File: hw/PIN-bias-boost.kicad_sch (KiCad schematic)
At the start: 9 parts, among them U2101 LT8330ES6-TRMPBF

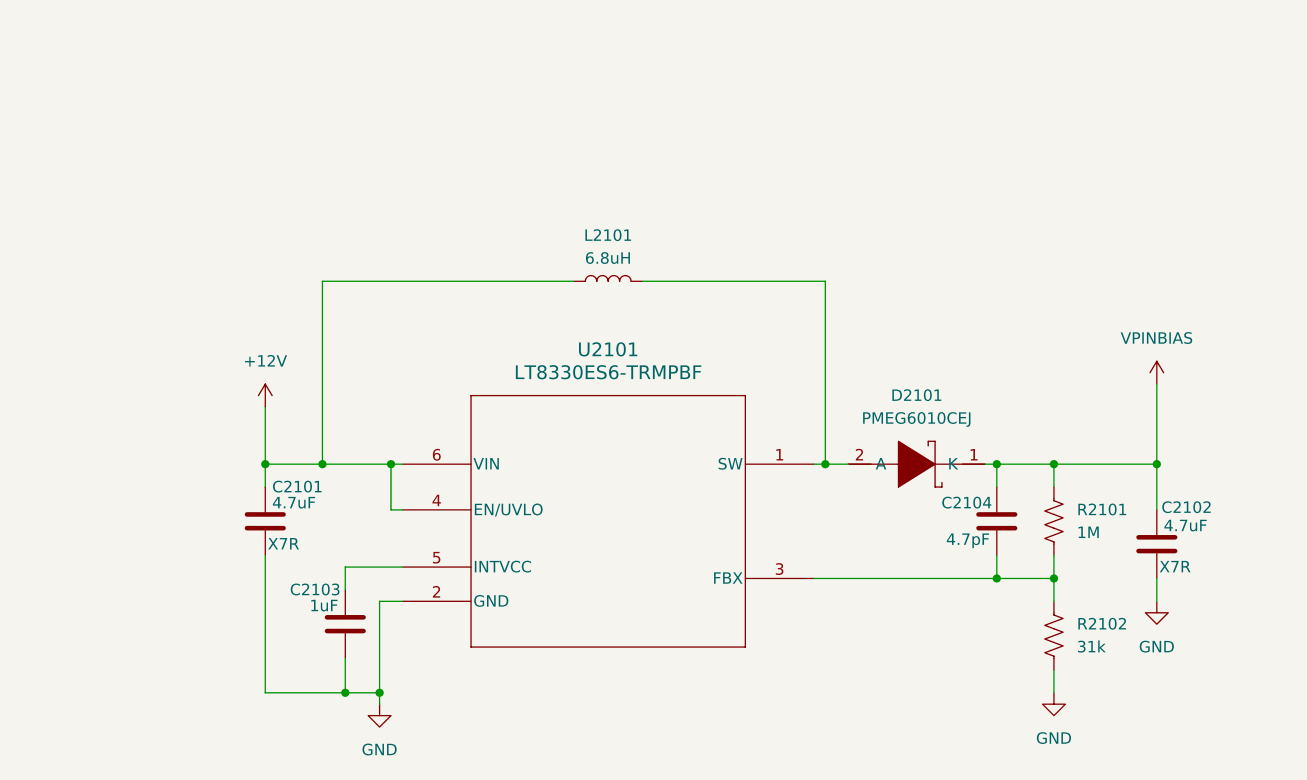
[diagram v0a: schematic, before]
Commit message: Add EER tank calculations stuff
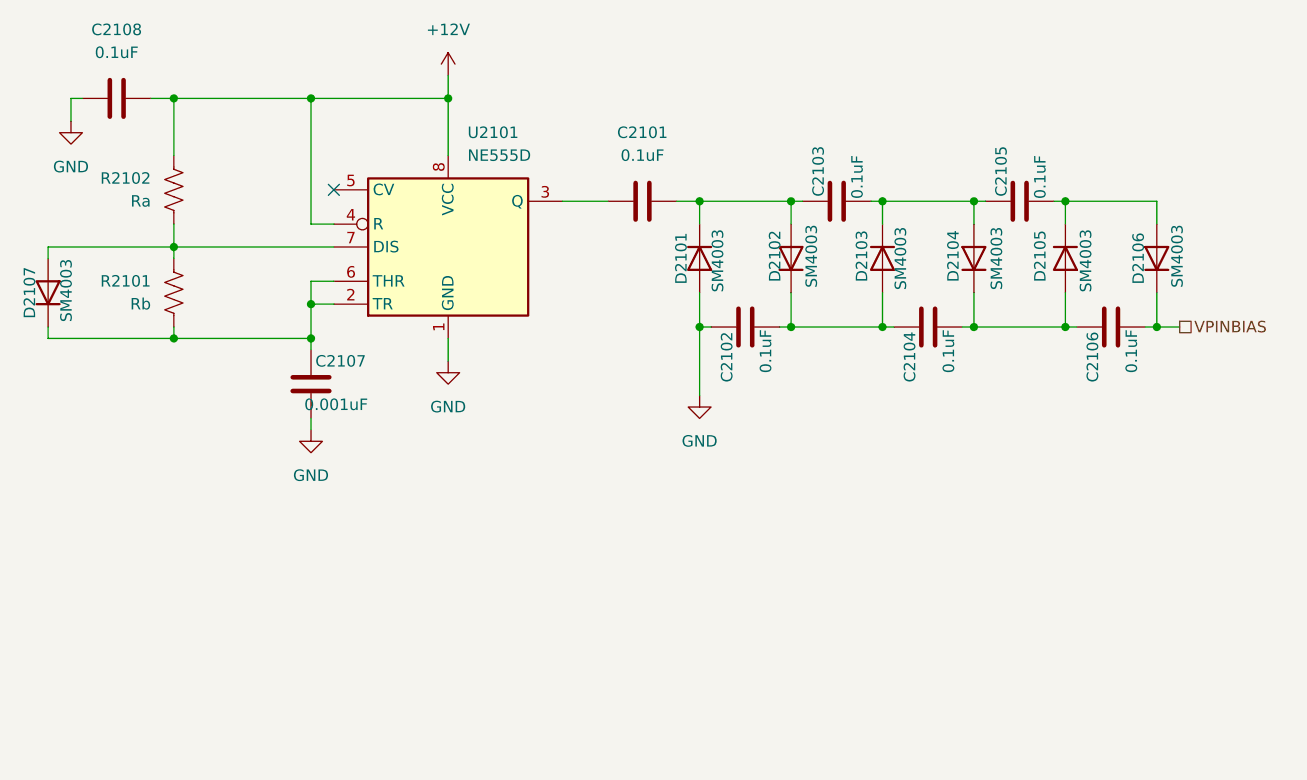
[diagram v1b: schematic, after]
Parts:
- removed D2101: PMEG6010CEJ, symbol USB-SSB-txcvr-altium-import:root_1_Df_TI WEBENCH
- removed L2101: 6.8uH, symbol Device:L
- removed U2101: LT8330ES6-TRMPBF, TSOT-23_S6_LIT, symbol LT8330ES6-TRMPBF:LT8330ES6-TRMPBF
- added C2105, C2106, C2108: 0.1uF, symbol Device:C
- added C2107: 0.001uF, symbol Device:C
- added D2101, D2102, D2103, D2104, D2105, D2106, D2107: SM4003, Diode_SMD:D_MELF, symbol Diode:SM4003
- added U2101: NE555D, Package_SO:SOIC-8_3.9x4.9mm_P1.27mm, symbol Timer:NE555D
- C2101, C2102: value 4.7uF -> 0.1uF; cap-type X7R -> (none)
- C2103: value 1uF -> 0.1uF
- C2104: value 4.7pF -> 0.1uF
- R2101: value 1M -> Rb
- R2102: value 31k -> Ra
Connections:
- net +12V: now also R2102.1, C2108.2, U2101.4 (R), U2101.8 (VCC); no longer C2101.1
- net GND: now also C2107.2, C2108.1, D2101.2 (A), U2101.1 (GND); no longer C2101.2, C2103.2, R2102.2
- net VPINBIAS: now also C2106.1, D2106.1 (K); no longer C2102.1, C2104.1, R2101.1
- net at C2103.1: now also C2105.2, D2103.1 (K), D2104.2 (A)
- new net: C2107.1, D2107.1 (K), R2101.2, U2101.2 (TR), U2101.6 (THR)
- new net: C2101.2, C2103.2, D2101.1 (K), D2102.2 (A)
- new net: D2107.2 (A), R2101.1, R2102.2, U2101.7 (DIS)
- new net: C2101.1, U2101.3 (Q)
- new net: C2104.1, C2106.2, D2104.1 (K), D2105.2 (A)
- new net: C2102.1, C2104.2, D2102.1 (K), D2103.2 (A)
- new net: C2105.1, D2105.1 (K), D2106.2 (A)
- no-connect marks 0 -> 1

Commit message: Tx LPF and its selection is pretty much done. Fix some OCD. Start to describe the design and construction.
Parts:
- renumbered C2108 to C2101, C2107 to C2102, C2101 to C2103, C2102 to C2104, C2103 to C2105, C2104 to C2106, C2105 to C2107, C2106 to C2108, D2107 to D2101, D2101 to D2102, D2102 to D2103, D2103 to D2104, D2104 to D2105, D2105 to D2106, D2106 to D2107, R2102 to R2101, R2101 to R2102
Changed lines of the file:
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@@
 		(on_board yes)
 		(dnp no)
-		(property "Reference" "C2107"
+		(property "Reference" "C2102"
 			(at 136.652 86.36 0)
 			(effects
@@
 			(project "USB-SSB-txcvr"
 				(path "/8ae46c04-d01a-4756-8774-512b694bfaff/cbf7569b-90aa-4e1a-84a7-d4153f6242b6/f249c9f1-932d-476f-a809-68b4c7a5d791"
-					(reference "C2107")
+					(reference "C2102")
 					(unit 1)
 				)
@@
 		(on_board yes)
 		(dnp no)
-		(property "Reference" "C2103"
+		(property "Reference" "C2105"
 			(at 189.738 68.072 0)
 			(effects
@@
 			(project "USB-SSB-txcvr"
 				(path "/8ae46c04-d01a-4756-8774-512b694bfaff/cbf7569b-90aa-4e1a-84a7-d4153f6242b6/f249c9f1-932d-476f-a809-68b4c7a5d791"
-					(reference "C2103")
+					(reference "C2105")
 					(unit 1)
 				)
@@
 		(on_board yes)
 		(dnp no)
-		(property "Reference" "D2107"
+		(property "Reference" "D2101"
 			(at 102.108 78.74 0)
 			(effects
@@
 			(project "USB-SSB-txcvr"
 				(path "/8ae46c04-d01a-4756-8774-512b694bfaff/cbf7569b-90aa-4e1a-84a7-d4153f6242b6/f249c9f1-932d-476f-a809-68b4c7a5d791"
-					(reference "D2107")
+					(reference "D2101")
 					(unit 1)
 				)
@@
 		(on_board yes)
 		(dnp no)
-		(property "Reference" "C2106"
+		(property "Reference" "C2108"
 			(at 220.218 83.058 0)
 			(effects
@@
 			(project "USB-SSB-txcvr"
 				(path "/8ae46c04-d01a-4756-8774-512b694bfaff/cbf7569b-90aa-4e1a-84a7-d4153f6242b6/f249c9f1-932d-476f-a809-68b4c7a5d791"
-					(reference "C2106")
+					(reference "C2108")
 					(unit 1)
 				)
@@
 		(dnp no)
 		(fields_autoplaced yes)
-		(property "Reference" "#PWR02102"
+		(property "Reference" "#PWR02103"
 			(at 148.59 58.42 0)
 			(effects
@@
 			(project ""
 				(path "/8ae46c04-d01a-4756-8774-512b694bfaff/cbf7569b-90aa-4e1a-84a7-d4153f6242b6/f249c9f1-932d-476f-a809-68b4c7a5d791"
-					(reference "#PWR02102")
+					(reference "#PWR02103")
 					(unit 1)
 				)
@@
 		(on_board yes)
 		(dnp no)
-		(property "Reference" "D2102"
+		(property "Reference" "D2103"
 			(at 184.912 74.676 0)
 			(effects
@@
 			(project "USB-SSB-txcvr"
 				(path "/8ae46c04-d01a-4756-8774-512b694bfaff/cbf7569b-90aa-4e1a-84a7-d4153f6242b6/f249c9f1-932d-476f-a809-68b4c7a5d791"
-					(reference "D2102")
+					(reference "D2103")
 					(unit 1)
 				)
@@
 		(on_board yes)
 		(dnp no)
-		(property "Reference" "D2106"
+		(property "Reference" "D2107"
 			(at 225.298 74.93 0)
 			(effects
@@
 			(project "USB-SSB-txcvr"
 				(path "/8ae46c04-d01a-4756-8774-512b694bfaff/cbf7569b-90aa-4e1a-84a7-d4153f6242b6/f249c9f1-932d-476f-a809-68b4c7a5d791"
-					(reference "D2106")
+					(reference "D2107")
 					(unit 1)
 				)
@@
 		(dnp no)
 		(fields_autoplaced yes)
-		(property "Reference" "#PWR02105"
+		(property "Reference" "#PWR02101"
 			(at 106.68 66.04 0)
 			(effects
@@
 			(project "USB-SSB-txcvr"
 				(path "/8ae46c04-d01a-4756-8774-512b694bfaff/cbf7569b-90aa-4e1a-84a7-d4153f6242b6/f249c9f1-932d-476f-a809-68b4c7a5d791"
-					(reference "#PWR02105")
+					(reference "#PWR02101")
 					(unit 1)
 				)
@@
 		(dnp no)
 		(fields_autoplaced yes)
-		(property "Reference" "C2101"
+		(property "Reference" "C2103"
 			(at 170.18 60.96 90)
 			(effects
@@
 			(project ""
 				(path "/8ae46c04-d01a-4756-8774-512b694bfaff/cbf7569b-90aa-4e1a-84a7-d4153f6242b6/f249c9f1-932d-476f-a809-68b4c7a5d791"
-					(reference "C2101")
+					(reference "C2103")
 					(unit 1)
 				)
@@
 		(on_board yes)
 		(dnp no)
-		(property "Reference" "C2104"
+		(property "Reference" "C2106"
 			(at 199.898 83.058 0)
 			(effects
@@
 			(project "USB-SSB-txcvr"
 				(path "/8ae46c04-d01a-4756-8774-512b694bfaff/cbf7569b-90aa-4e1a-84a7-d4153f6242b6/f249c9f1-932d-476f-a809-68b4c7a5d791"
-					(reference "C2104")
+					(reference "C2106")
 					(unit 1)
 				)
@@
 		(on_board yes)
 		(dnp no)
-		(property "Reference" "D2105"
+		(property "Reference" "D2106"
 			(at 214.376 74.676 0)
 			(effects
@@
 			(project "USB-SSB-txcvr"
 				(path "/8ae46c04-d01a-4756-8774-512b694bfaff/cbf7569b-90aa-4e1a-84a7-d4153f6242b6/f249c9f1-932d-476f-a809-68b4c7a5d791"
-					(reference "D2105")
+					(reference "D2106")
 					(unit 1)
 				)
@@
 		(on_board yes)
 		(dnp no)
-		(property "Reference" "D2103"
+		(property "Reference" "D2104"
 			(at 194.564 74.676 0)
 			(effects
@@
 			(project "USB-SSB-txcvr"
 				(path "/8ae46c04-d01a-4756-8774-512b694bfaff/cbf7569b-90aa-4e1a-84a7-d4153f6242b6/f249c9f1-932d-476f-a809-68b4c7a5d791"
-					(reference "D2103")
+					(reference "D2104")
 					(unit 1)
 				)
@@
 		(on_board yes)
 		(dnp no)
-		(property "Reference" "C2105"
+		(property "Reference" "C2107"
 			(at 210.058 68.072 0)
 			(effects
@@
 			(project "USB-SSB-txcvr"
 				(path "/8ae46c04-d01a-4756-8774-512b694bfaff/cbf7569b-90aa-4e1a-84a7-d4153f6242b6/f249c9f1-932d-476f-a809-68b4c7a5d791"
-					(reference "C2105")
+					(reference "C2107")
 					(unit 1)
 				)
@@
 		(on_board yes)
 		(dnp no)
-		(property "Reference" "D2101"
+		(property "Reference" "D2102"
 			(at 174.498 74.93 0)
 			(effects
@@
 			(project ""
 				(path "/8ae46c04-d01a-4756-8774-512b694bfaff/cbf7569b-90aa-4e1a-84a7-d4153f6242b6/f249c9f1-932d-476f-a809-68b4c7a5d791"
-					(reference "D2101")
+					(reference "D2102")
 					(unit 1)
 				)
@@
 		(dnp no)
 		(fields_autoplaced yes)
-		(property "Reference" "#PWR02101"
+		(property "Reference" "#PWR02105"
 			(at 176.53 96.52 0)
 			(effects
@@
 			(project ""
 				(path "/8ae46c04-d01a-4756-8774-512b694bfaff/cbf7569b-90aa-4e1a-84a7-d4153f6242b6/f249c9f1-932d-476f-a809-68b4c7a5d791"
-					(reference "#PWR02101")
+					(reference "#PWR02105")
 					(unit 1)
 				)
@@
 		(dnp no)
 		(fields_autoplaced yes)
-		(property "Reference" "#PWR02104"
+		(property "Reference" "#PWR02102"
 			(at 133.35 100.33 0)
 			(effects
@@
 			(project "USB-SSB-txcvr"
 				(path "/8ae46c04-d01a-4756-8774-512b694bfaff/cbf7569b-90aa-4e1a-84a7-d4153f6242b6/f249c9f1-932d-476f-a809-68b4c7a5d791"
-					(reference "#PWR02104")
+					(reference "#PWR02102")
 					(unit 1)
 				)
@@
 		(on_board yes)
 		(dnp no)
-		(property "Reference" "R2101"
+		(property "Reference" "R2102"
 			(at 115.57 77.4699 0)
 			(effects
@@
 			(project ""
 				(path "/8ae46c04-d01a-4756-8774-512b694bfaff/cbf7569b-90aa-4e1a-84a7-d4153f6242b6/f249c9f1-932d-476f-a809-68b4c7a5d791"
-					(reference "R2101")
+					(reference "R2102")
 					(unit 1)
 				)
@@
 		(dnp no)
 		(fields_autoplaced yes)
-		(property "Reference" "#PWR02103"
+		(property "Reference" "#PWR02104"
 			(at 148.59 92.71 0)
 			(effects
@@
 			(project "USB-SSB-txcvr"
 				(path "/8ae46c04-d01a-4756-8774-512b694bfaff/cbf7569b-90aa-4e1a-84a7-d4153f6242b6/f249c9f1-932d-476f-a809-68b4c7a5d791"
-					(reference "#PWR02103")
+					(reference "#PWR02104")
 					(unit 1)
 				)
@@
 		(on_board yes)
 		(dnp no)
-		(property "Reference" "C2102"
+		(property "Reference" "C2104"
 			(at 179.578 83.058 0)
 			(effects
@@
 			(project "USB-SSB-txcvr"
 				(path "/8ae46c04-d01a-4756-8774-512b694bfaff/cbf7569b-90aa-4e1a-84a7-d4153f6242b6/f249c9f1-932d-476f-a809-68b4c7a5d791"
-					(reference "C2102")
+					(reference "C2104")
 					(unit 1)
 				)
@@
 		(on_board yes)
 		(dnp no)
-		(property "Reference" "D2104"
+		(property "Reference" "D2105"
 			(at 204.724 74.676 0)
 			(effects
@@
 			(project "USB-SSB-txcvr"
 				(path "/8ae46c04-d01a-4756-8774-512b694bfaff/cbf7569b-90aa-4e1a-84a7-d4153f6242b6/f249c9f1-932d-476f-a809-68b4c7a5d791"
-					(reference "D2104")
+					(reference "D2105")
 					(unit 1)
 				)
@@
 		(on_board yes)
 		(dnp no)
-		(property "Reference" "R2102"
+		(property "Reference" "R2101"
 			(at 115.57 66.0399 0)
 			(effects
@@
 			(project "USB-SSB-txcvr"
 				(path "/8ae46c04-d01a-4756-8774-512b694bfaff/cbf7569b-90aa-4e1a-84a7-d4153f6242b6/f249c9f1-932d-476f-a809-68b4c7a5d791"
-					(reference "R2102")
+					(reference "R2101")
 					(unit 1)
 				)
@@
 		(dnp no)
 		(fields_autoplaced yes)
-		(property "Reference" "C2108"
+		(property "Reference" "C2101"
 			(at 111.76 49.53 90)
 			(effects
@@
 			(project "USB-SSB-txcvr"
 				(path "/8ae46c04-d01a-4756-8774-512b694bfaff/cbf7569b-90aa-4e1a-84a7-d4153f6242b6/f249c9f1-932d-476f-a809-68b4c7a5d791"
-					(reference "C2108")
-					(unit 1)
-				)
+					(reference "C2101")
+					(unit 1)
+				)

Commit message: Embarking on a whole new arch for rx without BPFs and using a single digitally tuned tank plus three QSDs to accomplish image rejection in digital domain
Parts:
- renumbered C2101 to C2001, C2102 to C2002, C2103 to C2003, C2104 to C2004, C2105 to C2005, C2106 to C2006, C2107 to C2007, C2108 to C2008, D2101 to D2001, D2102 to D2002, D2103 to D2003, D2104 to D2004, D2105 to D2005, D2106 to D2006, D2107 to D2007, R2101 to R2001, R2102 to R2002, U2101 to U2001
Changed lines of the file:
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@@
 		(on_board yes)
 		(dnp no)
-		(property "Reference" "C2102"
+		(property "Reference" "C2002"
 			(at 136.652 86.36 0)
 			(effects
@@
 			(project "USB-SSB-txcvr"
 				(path "/8ae46c04-d01a-4756-8774-512b694bfaff/cbf7569b-90aa-4e1a-84a7-d4153f6242b6/f249c9f1-932d-476f-a809-68b4c7a5d791"
-					(reference "C2102")
+					(reference "C2002")
 					(unit 1)
 				)
@@
 		(on_board yes)
 		(dnp no)
-		(property "Reference" "C2105"
+		(property "Reference" "C2005"
 			(at 189.738 68.072 0)
 			(effects
@@
 			(project "USB-SSB-txcvr"
 				(path "/8ae46c04-d01a-4756-8774-512b694bfaff/cbf7569b-90aa-4e1a-84a7-d4153f6242b6/f249c9f1-932d-476f-a809-68b4c7a5d791"
-					(reference "C2105")
+					(reference "C2005")
 					(unit 1)
 				)
@@
 		(on_board yes)
 		(dnp no)
-		(property "Reference" "D2101"
+		(property "Reference" "D2001"
 			(at 102.108 78.74 0)
 			(effects
@@
 			(project "USB-SSB-txcvr"
 				(path "/8ae46c04-d01a-4756-8774-512b694bfaff/cbf7569b-90aa-4e1a-84a7-d4153f6242b6/f249c9f1-932d-476f-a809-68b4c7a5d791"
-					(reference "D2101")
+					(reference "D2001")
 					(unit 1)
 				)
@@
 		(dnp no)
 		(fields_autoplaced yes)
-		(property "Reference" "U2101"
+		(property "Reference" "U2001"
 			(at 150.7333 60.96 0)
 			(effects
@@
 			(project ""
 				(path "/8ae46c04-d01a-4756-8774-512b694bfaff/cbf7569b-90aa-4e1a-84a7-d4153f6242b6/f249c9f1-932d-476f-a809-68b4c7a5d791"
-					(reference "U2101")
+					(reference "U2001")
 					(unit 1)
 				)
@@
 		(on_board yes)
 		(dnp no)
-		(property "Reference" "C2108"
+		(property "Reference" "C2008"
 			(at 220.218 83.058 0)
 			(effects
@@
 			(project "USB-SSB-txcvr"
 				(path "/8ae46c04-d01a-4756-8774-512b694bfaff/cbf7569b-90aa-4e1a-84a7-d4153f6242b6/f249c9f1-932d-476f-a809-68b4c7a5d791"
-					(reference "C2108")
+					(reference "C2008")
 					(unit 1)
 				)
@@
 		(dnp no)
 		(fields_autoplaced yes)
-		(property "Reference" "#PWR02103"
+		(property "Reference" "#PWR02003"
 			(at 148.59 58.42 0)
 			(effects
@@
 			(project ""
 				(path "/8ae46c04-d01a-4756-8774-512b694bfaff/cbf7569b-90aa-4e1a-84a7-d4153f6242b6/f249c9f1-932d-476f-a809-68b4c7a5d791"
-					(reference "#PWR02103")
+					(reference "#PWR02003")
 					(unit 1)
 				)
@@
 		(on_board yes)
 		(dnp no)
-		(property "Reference" "D2103"
+		(property "Reference" "D2003"
 			(at 184.912 74.676 0)
 			(effects
@@
 			(project "USB-SSB-txcvr"
 				(path "/8ae46c04-d01a-4756-8774-512b694bfaff/cbf7569b-90aa-4e1a-84a7-d4153f6242b6/f249c9f1-932d-476f-a809-68b4c7a5d791"
-					(reference "D2103")
+					(reference "D2003")
 					(unit 1)
 				)
@@
 		(on_board yes)
 		(dnp no)
-		(property "Reference" "D2107"
+		(property "Reference" "D2007"
 			(at 225.298 74.93 0)
 			(effects
@@
 			(project "USB-SSB-txcvr"
 				(path "/8ae46c04-d01a-4756-8774-512b694bfaff/cbf7569b-90aa-4e1a-84a7-d4153f6242b6/f249c9f1-932d-476f-a809-68b4c7a5d791"
-					(reference "D2107")
+					(reference "D2007")
 					(unit 1)
 				)
@@
 		(dnp no)
 		(fields_autoplaced yes)
-		(property "Reference" "#PWR02101"
+		(property "Reference" "#PWR02001"
 			(at 106.68 66.04 0)
 			(effects
@@
 			(project "USB-SSB-txcvr"
 				(path "/8ae46c04-d01a-4756-8774-512b694bfaff/cbf7569b-90aa-4e1a-84a7-d4153f6242b6/f249c9f1-932d-476f-a809-68b4c7a5d791"
-					(reference "#PWR02101")
+					(reference "#PWR02001")
 					(unit 1)
 				)
@@
 		(dnp no)
 		(fields_autoplaced yes)
-		(property "Reference" "C2103"
+		(property "Reference" "C2003"
 			(at 170.18 60.96 90)
 			(effects
@@
 			(project ""
 				(path "/8ae46c04-d01a-4756-8774-512b694bfaff/cbf7569b-90aa-4e1a-84a7-d4153f6242b6/f249c9f1-932d-476f-a809-68b4c7a5d791"
-					(reference "C2103")
+					(reference "C2003")
 					(unit 1)
 				)
@@
 		(on_board yes)
 		(dnp no)
-		(property "Reference" "C2106"
+		(property "Reference" "C2006"
 			(at 199.898 83.058 0)
 			(effects
@@
 			(project "USB-SSB-txcvr"
 				(path "/8ae46c04-d01a-4756-8774-512b694bfaff/cbf7569b-90aa-4e1a-84a7-d4153f6242b6/f249c9f1-932d-476f-a809-68b4c7a5d791"
-					(reference "C2106")
+					(reference "C2006")
 					(unit 1)
 				)
@@
 		(on_board yes)
 		(dnp no)
-		(property "Reference" "D2106"
+		(property "Reference" "D2006"
 			(at 214.376 74.676 0)
 			(effects
@@
 			(project "USB-SSB-txcvr"
 				(path "/8ae46c04-d01a-4756-8774-512b694bfaff/cbf7569b-90aa-4e1a-84a7-d4153f6242b6/f249c9f1-932d-476f-a809-68b4c7a5d791"
-					(reference "D2106")
+					(reference "D2006")
 					(unit 1)
 				)
@@
 		(on_board yes)
 		(dnp no)
-		(property "Reference" "D2104"
+		(property "Reference" "D2004"
 			(at 194.564 74.676 0)
 			(effects
@@
 			(project "USB-SSB-txcvr"
 				(path "/8ae46c04-d01a-4756-8774-512b694bfaff/cbf7569b-90aa-4e1a-84a7-d4153f6242b6/f249c9f1-932d-476f-a809-68b4c7a5d791"
-					(reference "D2104")
+					(reference "D2004")
 					(unit 1)
 				)
@@
 		(on_board yes)
 		(dnp no)
-		(property "Reference" "C2107"
+		(property "Reference" "C2007"
 			(at 210.058 68.072 0)
 			(effects
@@
 			(project "USB-SSB-txcvr"
 				(path "/8ae46c04-d01a-4756-8774-512b694bfaff/cbf7569b-90aa-4e1a-84a7-d4153f6242b6/f249c9f1-932d-476f-a809-68b4c7a5d791"
-					(reference "C2107")
+					(reference "C2007")
 					(unit 1)
 				)
@@
 		(on_board yes)
 		(dnp no)
-		(property "Reference" "D2102"
+		(property "Reference" "D2002"
 			(at 174.498 74.93 0)
 			(effects
@@
 			(project ""
 				(path "/8ae46c04-d01a-4756-8774-512b694bfaff/cbf7569b-90aa-4e1a-84a7-d4153f6242b6/f249c9f1-932d-476f-a809-68b4c7a5d791"
-					(reference "D2102")
+					(reference "D2002")
 					(unit 1)
 				)
@@
 		(dnp no)
 		(fields_autoplaced yes)
-		(property "Reference" "#PWR02105"
+		(property "Reference" "#PWR02005"
 			(at 176.53 96.52 0)
 			(effects
@@
 			(project ""
 				(path "/8ae46c04-d01a-4756-8774-512b694bfaff/cbf7569b-90aa-4e1a-84a7-d4153f6242b6/f249c9f1-932d-476f-a809-68b4c7a5d791"
-					(reference "#PWR02105")
+					(reference "#PWR02005")
 					(unit 1)
 				)
@@
 		(dnp no)
 		(fields_autoplaced yes)
-		(property "Reference" "#PWR02102"
+		(property "Reference" "#PWR02002"
 			(at 133.35 100.33 0)
 			(effects
@@
 			(project "USB-SSB-txcvr"
 				(path "/8ae46c04-d01a-4756-8774-512b694bfaff/cbf7569b-90aa-4e1a-84a7-d4153f6242b6/f249c9f1-932d-476f-a809-68b4c7a5d791"
-					(reference "#PWR02102")
+					(reference "#PWR02002")
 					(unit 1)
 				)
@@
 		(on_board yes)
 		(dnp no)
-		(property "Reference" "R2102"
+		(property "Reference" "R2002"
 			(at 115.57 77.4699 0)
 			(effects
@@
 			(project ""
 				(path "/8ae46c04-d01a-4756-8774-512b694bfaff/cbf7569b-90aa-4e1a-84a7-d4153f6242b6/f249c9f1-932d-476f-a809-68b4c7a5d791"
-					(reference "R2102")
+					(reference "R2002")
 					(unit 1)
 				)
@@
 		(dnp no)
 		(fields_autoplaced yes)
-		(property "Reference" "#PWR02104"
+		(property "Reference" "#PWR02004"
 			(at 148.59 92.71 0)
 			(effects
@@
 			(project "USB-SSB-txcvr"
 				(path "/8ae46c04-d01a-4756-8774-512b694bfaff/cbf7569b-90aa-4e1a-84a7-d4153f6242b6/f249c9f1-932d-476f-a809-68b4c7a5d791"
-					(reference "#PWR02104")
+					(reference "#PWR02004")
 					(unit 1)
 				)
@@
 		(on_board yes)
 		(dnp no)
-		(property "Reference" "C2104"
+		(property "Reference" "C2004"
 			(at 179.578 83.058 0)
 			(effects
@@
 			(project "USB-SSB-txcvr"
 				(path "/8ae46c04-d01a-4756-8774-512b694bfaff/cbf7569b-90aa-4e1a-84a7-d4153f6242b6/f249c9f1-932d-476f-a809-68b4c7a5d791"
-					(reference "C2104")
+					(reference "C2004")
 					(unit 1)
 				)
@@
 		(on_board yes)
 		(dnp no)
-		(property "Reference" "D2105"
+		(property "Reference" "D2005"
 			(at 204.724 74.676 0)
 			(effects
@@
 			(project "USB-SSB-txcvr"
 				(path "/8ae46c04-d01a-4756-8774-512b694bfaff/cbf7569b-90aa-4e1a-84a7-d4153f6242b6/f249c9f1-932d-476f-a809-68b4c7a5d791"
-					(reference "D2105")
+					(reference "D2005")
 					(unit 1)
 				)
@@
 		(on_board yes)
 		(dnp no)
-		(property "Reference" "R2101"
+		(property "Reference" "R2001"
 			(at 115.57 66.0399 0)
 			(effects
@@
 			(project "USB-SSB-txcvr"
 				(path "/8ae46c04-d01a-4756-8774-512b694bfaff/cbf7569b-90aa-4e1a-84a7-d4153f6242b6/f249c9f1-932d-476f-a809-68b4c7a5d791"
-					(reference "R2101")
+					(reference "R2001")
 					(unit 1)
 				)
@@
 		(dnp no)
 		(fields_autoplaced yes)
-		(property "Reference" "C2101"
+		(property "Reference" "C2001"
 			(at 111.76 49.53 90)
 			(effects
@@
 			(project "USB-SSB-txcvr"
 				(path "/8ae46c04-d01a-4756-8774-512b694bfaff/cbf7569b-90aa-4e1a-84a7-d4153f6242b6/f249c9f1-932d-476f-a809-68b4c7a5d791"
-					(reference "C2101")
-					(unit 1)
-				)
+					(reference "C2001")
+					(unit 1)
+				)
